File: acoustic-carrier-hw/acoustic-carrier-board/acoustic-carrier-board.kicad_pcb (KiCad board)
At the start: 6 copper layers, 99 x 97 mm, 363 parts, among them IC1 ECP5-BGA256, IC1101 MT41K256M16TW-107_P, J1001 BWU.FL-IPEX1, J1002 BWU.FL-IPEX1, J1003 BWU.FL-IPEX1, J1005 BWU.FL-IPEX1, J1006 BWU.FL-IPEX1, J1007 8P8C_Shielded, J1008 BWU.FL-IPEX1, J1009 BWU.FL-IPEX1, J1010 BWU.FL-IPEX1, J1201 HR911130A, J201 Conn_02x06_Odd_Even, J701 Conn_02x03_Odd_Even, J702 PMOD_JTAG, J703 PMOD_SPI, J704 PMOD_GPIO, J801 TYPE-C-31-M-12, J903 Conn_02x06_Odd_Even, Q201 AO3401A, U1001 MS9280, U1002 THS4521IDGK, U1003 DGQ2788AEN-T1-GE4, U1004 LMV321, U1005 TL432DBZ, U1201 KSZ9031RN, U201 TPS2121RUX, U202 TLV62569DBV, U203 TLV62569DBV, U204 TLV62569DBV, U205 TLV62569DBV, U206 OPA376xxDBV, U701 W25Q128JVS, U702 W25Q128JVS, U801 USB3300-EZK, U802 LMV321, Y1201 25MHz, Y401 Crystal Oscillator, Y801 Crystal_GND24_Small

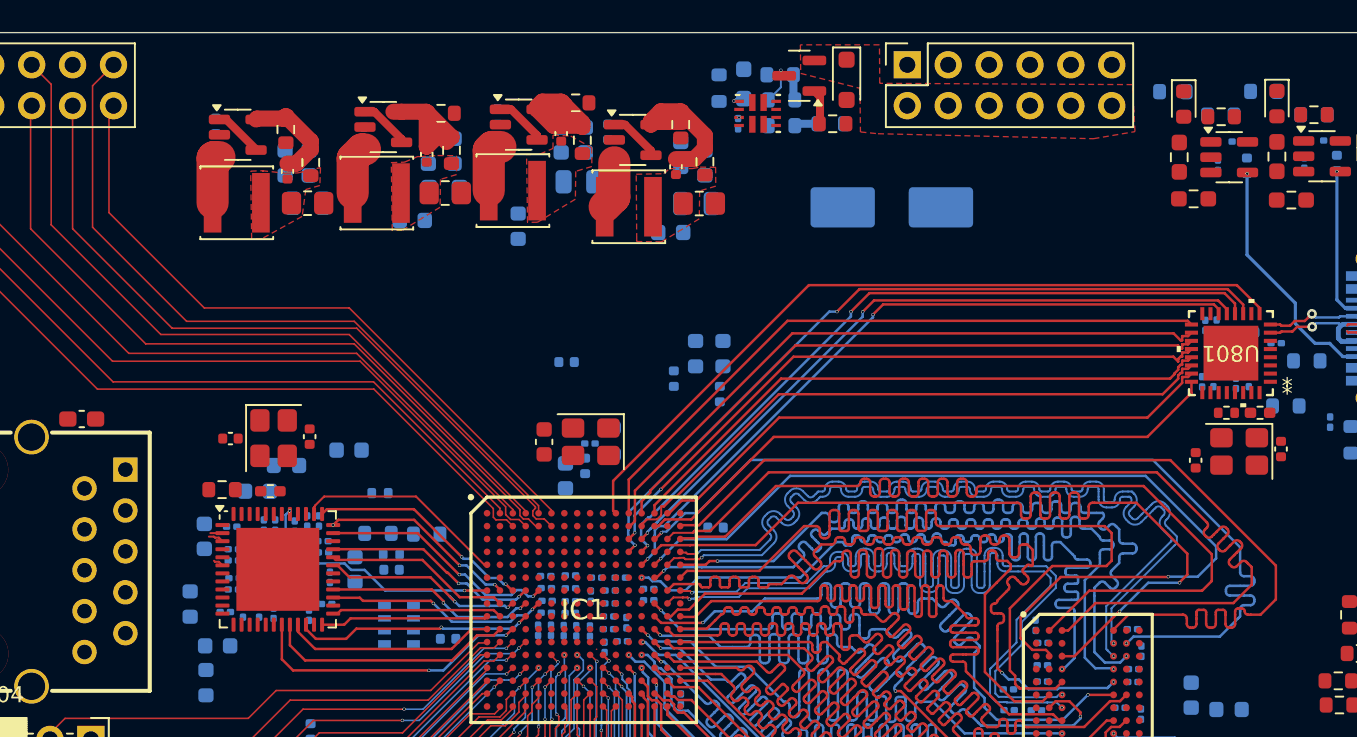
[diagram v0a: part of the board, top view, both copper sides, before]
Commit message: [carrier] rerouted USB ULP traces (next) add power planes
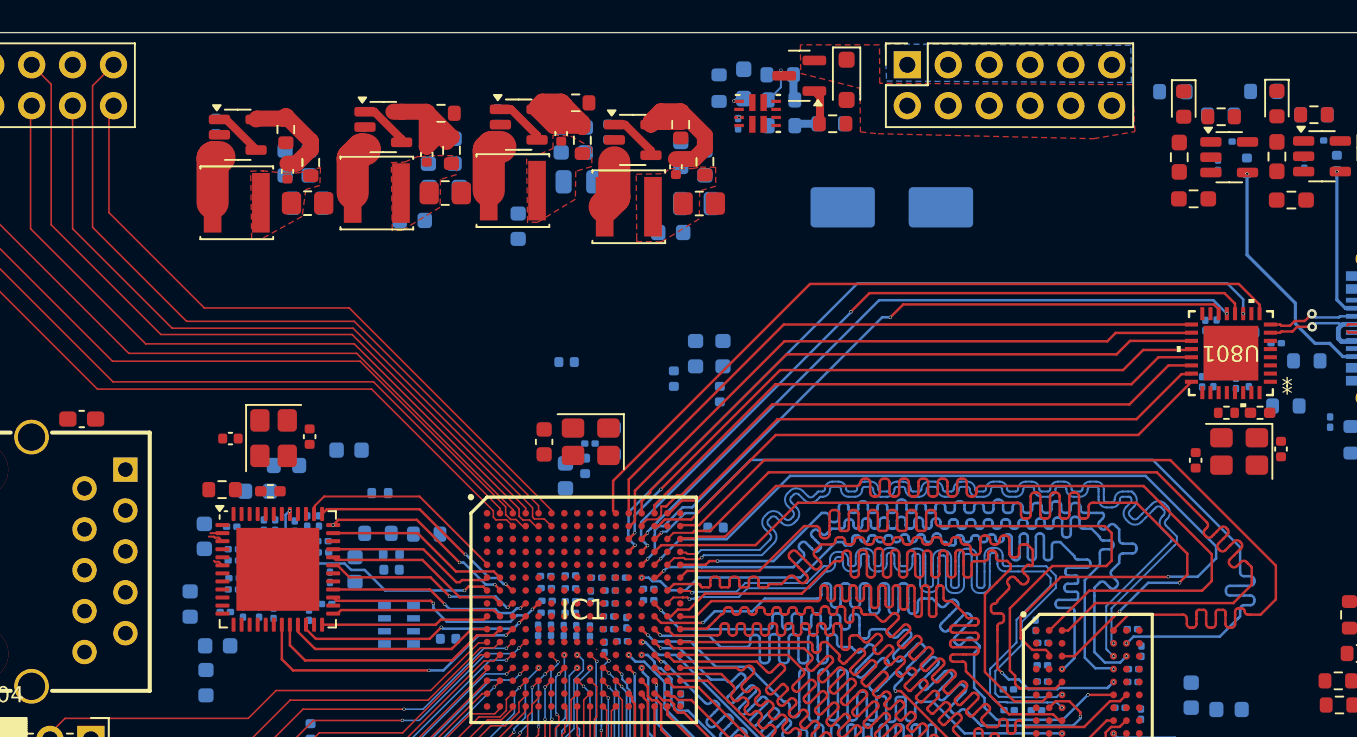
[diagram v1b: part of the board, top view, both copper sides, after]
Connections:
- IC1 pad F1: unconnected-(IC1G-PL14A/LDQ20-PadF1) -> /RGMII_RX.CTL
- IC1 pad F2: unconnected-(IC1G-PL11C-PadF2) -> /RGMII_RX.CLK
- IC1 pad G4: /RGMII_RX.CTL -> unconnected-(IC1G-PL11B-PadG4)
- IC1 pad G5: /RGMII_RX.CLK -> unconnected-(IC1G-PL11A-PadG5)
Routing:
- net /RGMII_RX.CLK: track 14.8 -> 11.5 mm, vias 2 -> 0
- net /RGMII_RX.CTL: track 13.5 -> 10.5 mm, vias 2 -> 0
- net /RGMII_RX.D1: track 13.3 -> 12.3 mm
- net /USB.D5: track 39.7 -> 39.1 mm
- net /USB.D6: track 41.5 -> 41.0 mm
- added copper zone on B.Cu, net GND

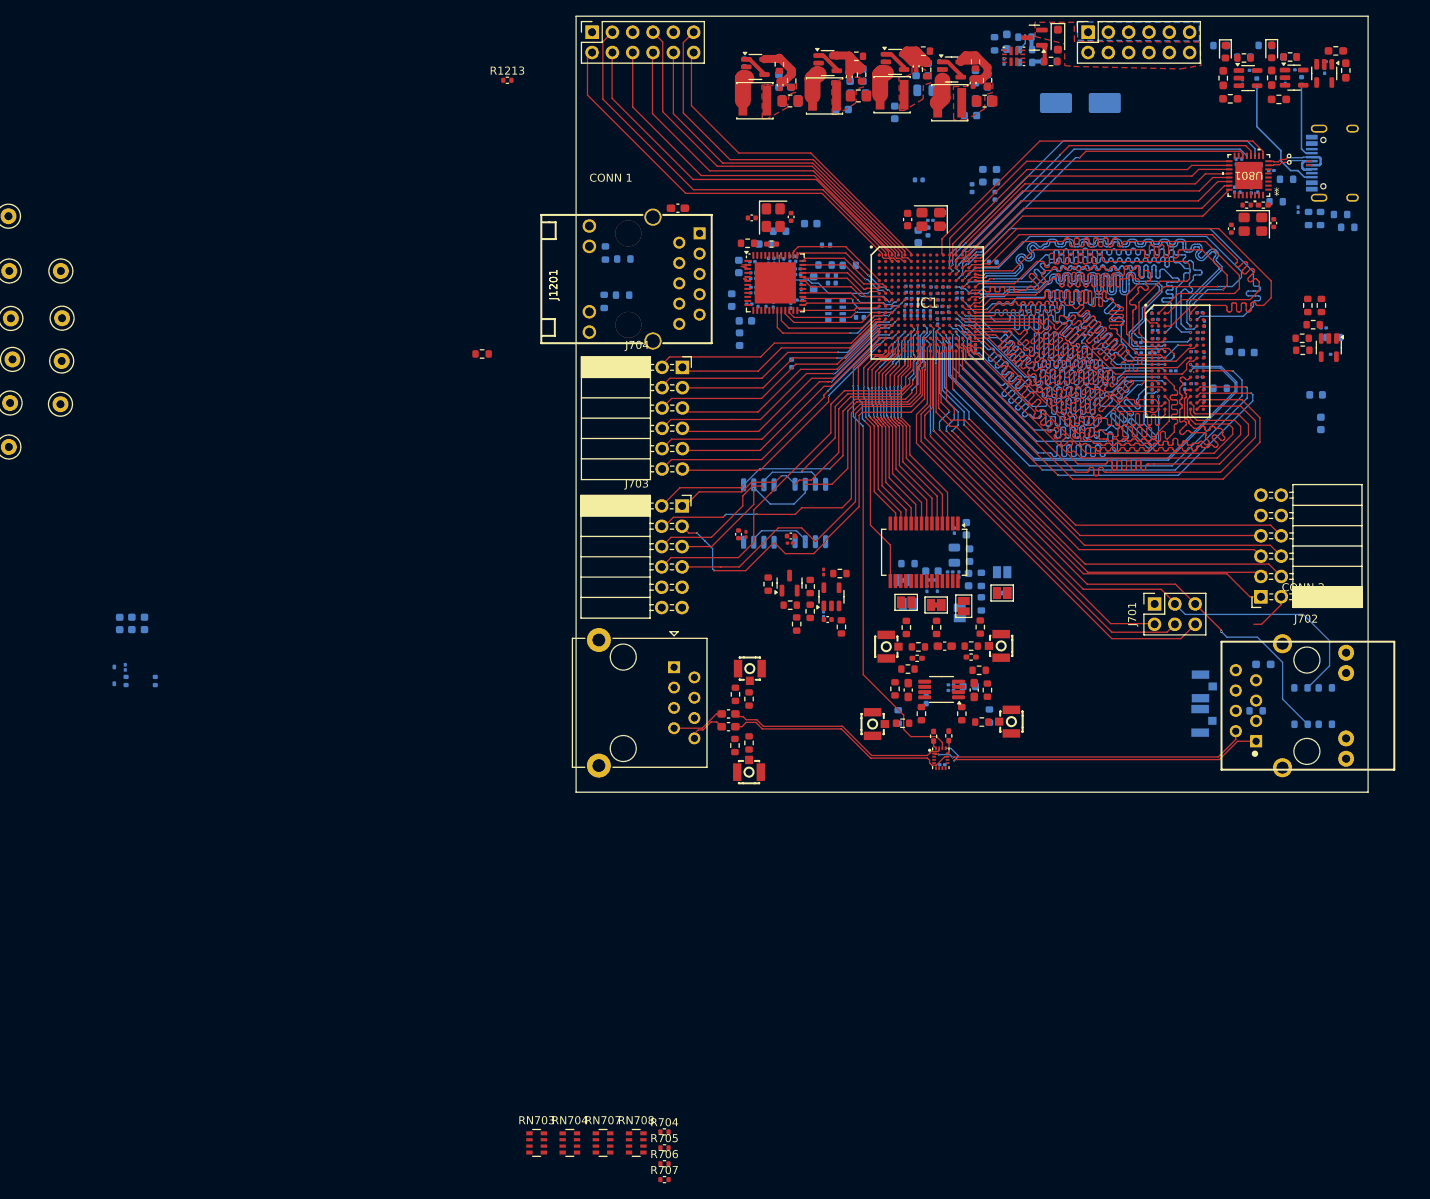
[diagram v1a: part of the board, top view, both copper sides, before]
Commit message: [carrier] Starting on power planes
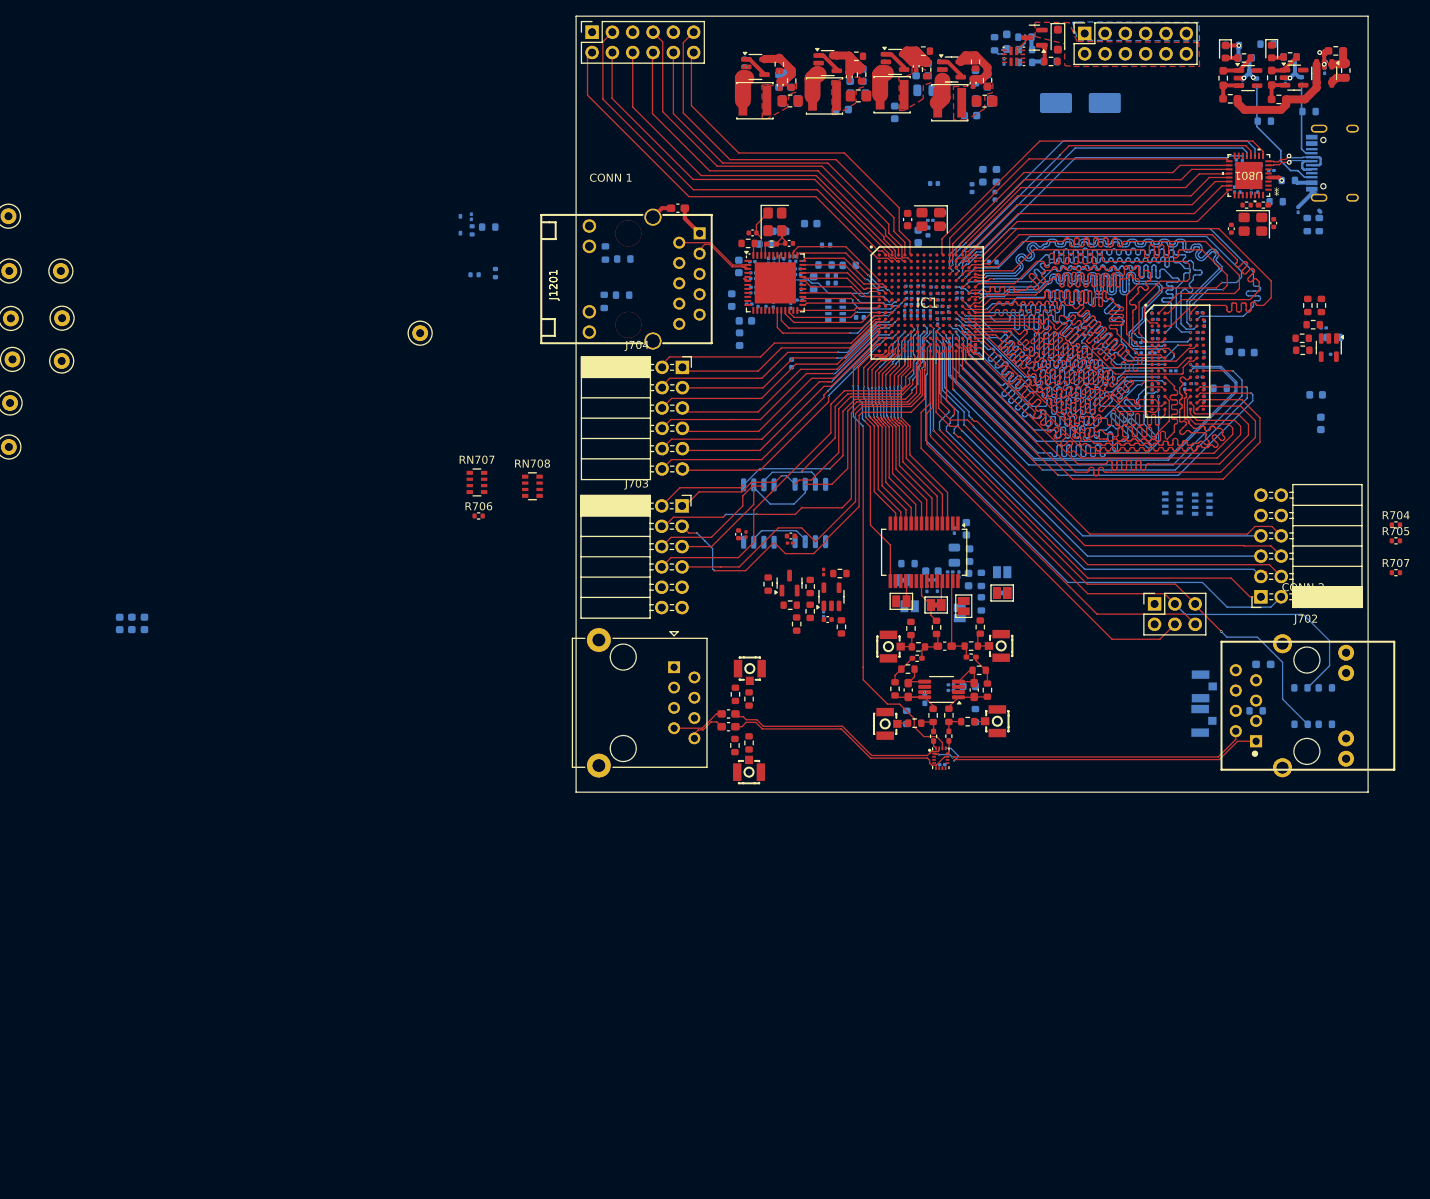
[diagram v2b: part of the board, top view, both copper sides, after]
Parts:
- R1213, R602, RN703, RN704: moved to B.Cu
- moved R704 118.8 mm to (147.5, 115.6)
- moved R707 118.8 mm to (147.5, 121.6)
- moved R705 118.8 mm to (147.5, 117.6)
- moved RN703 112.8 mm to (119.5, 112.8)
- moved RN704 112.4 mm to (123.3, 113.0), turned to 180 degrees
- moved R706 84.2 mm to (32.8, 114.5)
- moved RN707 84.1 mm to (32.6, 110.3)
- moved RN708 83.1 mm to (39.5, 110.8)
- moved C1229 71.0 mm to (31.9, 77.1)
- moved D1201 71.0 mm to (30.5, 78.1)
- moved R1212 71.0 mm to (32.0, 78.8)
- moved R1208 66.4 mm to (34.9, 84.1)
- moved TP1201 45.8 mm to (25.5, 91.6)
- moved R1213 24.7 mm to (32.3, 84.3)
- moved R804 16.9 mm to (131.0, 65.1)
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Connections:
- J701 pad 2: /FPGA-CONFIG-FLASH/FPGA_DONE -> VCORE_3V3
- J701 pad 6: /FPGA-CONFIG-FLASH/FPGA_RESET -> /FPGA-CONFIG-FLASH/FPGA_DONE
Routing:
- net GND: track 0.00 -> 24.6 mm, vias 0 -> 9
- net /USB-PHY/USBCC_VREF_BUFF: track 0.00 -> 15.2 mm
- net /ANALOG-FRONTEND/ADC_AIN+: track 0.00 -> 11.3 mm
- net /ETHERNET-PHY/ETH_PHY_A+: track 0.75 -> 9.74 mm
- net /ETHERNET-PHY/ETH_PHY_A-: track 0.96 -> 9.01 mm
- net Net-(U1002-+): track 0.00 -> 7.75 mm
- net Net-(U1201-XI): track 0.00 -> 6.15 mm
- net Net-(C1012-Pad1): track 0.00 -> 6.09 mm
- net /ANALOG-FRONTEND/ADC_REFTS: track 0.00 -> 5.74 mm
- net Net-(U1002--): track 0.00 -> 5.57 mm
- net /FPGA-CONFIG-FLASH/FPGA_DONE: track 51.5 -> 56.7 mm
- net Net-(C1228-Pad2): track 0.00 -> 4.87 mm
- net /ANALOG-FRONTEND/ADC_AIN-: track 0.00 -> 4.81 mm
- net /POWER/USB_VBUS: track 0.00 -> 4.22 mm
- net Net-(C1016-Pad2): track 0.00 -> 4.22 mm
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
